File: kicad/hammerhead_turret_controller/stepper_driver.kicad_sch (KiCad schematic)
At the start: 16 parts, among them U10 A4988SETTR-T

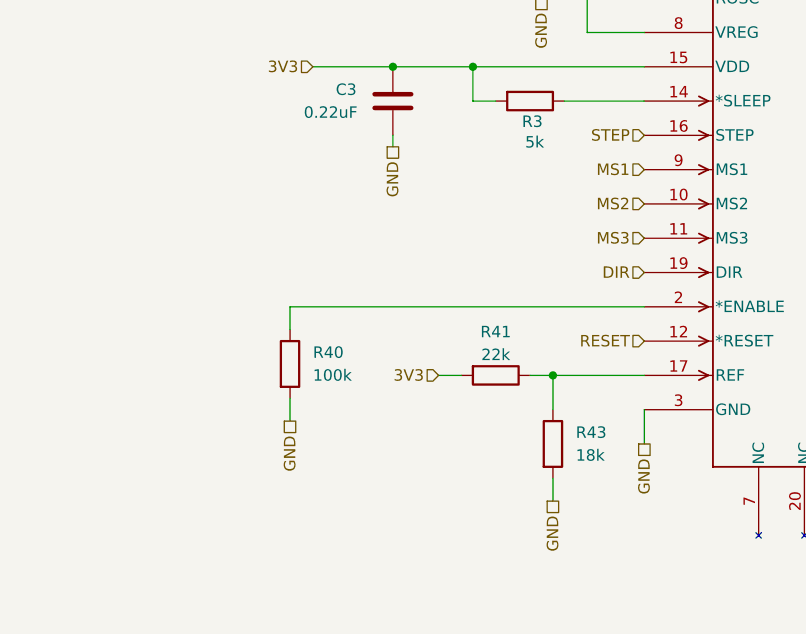
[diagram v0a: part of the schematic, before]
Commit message: add can transceiver
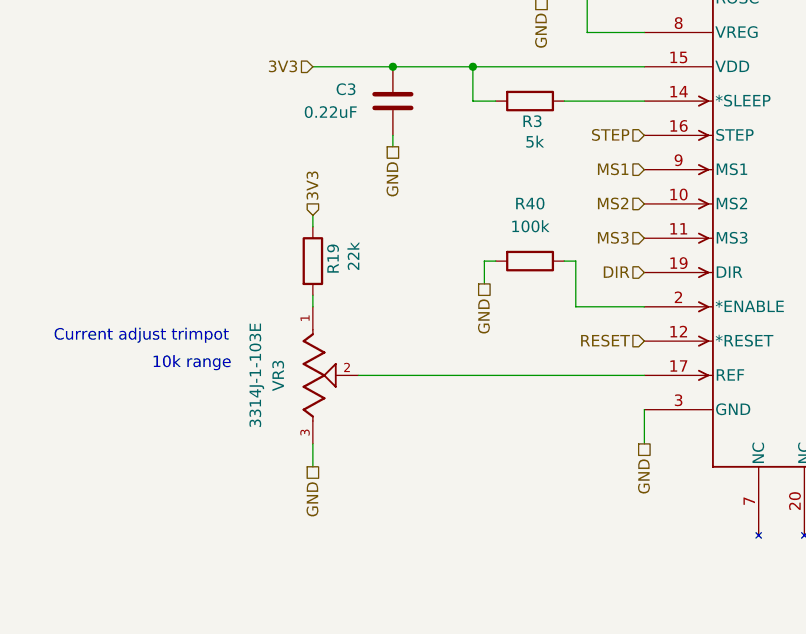
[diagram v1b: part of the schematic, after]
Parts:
- removed R41: 22k, Resistor_SMD:R_0201_0603Metric, symbol Device:R
- removed R43: 18k, Resistor_SMD:R_0201_0603Metric, symbol Device:R
- added R19: 22k, Resistor_SMD:R_0201_0603Metric, symbol Device:R
- added VR3: 3314J-1-103E, 3314J-1-103E:TRIM_3314J-1-103E, symbol 3314J-1-103E:3314J-1-103E
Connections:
- net 3V3: now also R19.1
- net GND: now also VR3.3
- net at U10.17 (REF): now also VR3.2
- new net: R19.2, VR3.1
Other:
- note added: "10k range"
- note added: "Current adjust trimpot"
- moved on the sheet: R40
